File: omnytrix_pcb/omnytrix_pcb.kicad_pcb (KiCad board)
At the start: 2 copper layers, 38 x 45.5 mm, 37 parts, among them J1 Conn_01x07, J2 Micro_SD_Card_Det2, J3 Conn_01x02, J4 USB_C_Receptacle_PowerOnly_6P, SW1 SW_Push, U1 LD3985M33R_SOT23, U2 TP4056, U3 STM32F411RCTx, U4 FS8205A, U5 DW01

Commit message: add ground filled zone
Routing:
- net GND: vias 12 -> 32
- added copper zone on B.Cu, net GND
- added copper zone on F.Cu, net GND
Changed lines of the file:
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@@
   (segment (start 88.190736 105.434962) (end 85.731126 105.434962) (width 0.5) (layer "F.Cu") (net 2))
   (via (at 95.33886 94.532757) (size 0.8) (drill 0.4) (layers "F.Cu" "B.Cu") (net 2))
+  (via (at 83.455723 106.615239) (size 0.8) (drill 0.4) (layers "F.Cu" "B.Cu") (free) (net 2))
+  (via (at 85.177509 90.32317) (size 0.8) (drill 0.4) (layers "F.Cu" "B.Cu") (free) (net 2))
+  (via (at 112.594438 89.521213) (size 0.8) (drill 0.4) (layers "F.Cu" "B.Cu") (free) (net 2))
   (via (at 96.706297 116.206286) (size 0.8) (drill 0.4) (layers "F.Cu" "B.Cu") (net 2))
+  (via (at 98.209321 82.905062) (size 0.8) (drill 0.4) (layers "F.Cu" "B.Cu") (free) (net 2))
+  (via (at 104.166757 95.184021) (size 0.8) (drill 0.4) (layers "F.Cu" "B.Cu") (free) (net 2))
+  (via (at 89.939833 118.060929) (size 0.8) (drill 0.4) (layers "F.Cu" "B.Cu") (free) (net 2))
+  (via (at 109.855 118.745) (size 0.8) (drill 0.4) (layers "F.Cu" "B.Cu") (free) (net 2))
+  (via (at 110.890277 86.864728) (size 0.8) (drill 0.4) (layers "F.Cu" "B.Cu") (free) (net 2))
+  (via (at 102.01862 83.957631) (size 0.8) (drill 0.4) (layers "F.Cu" "B.Cu") (free) (net 2))
   (via (at 102.395827 116.206286) (size 0.8) (drill 0.4) (layers "F.Cu" "B.Cu") (net 2))
+  (via (at 107.95 85.725) (size 0.8) (drill 0.4) (layers "F.Cu" "B.Cu") (free) (net 2))
+  (via (at 108.654941 107.256118) (size 0.8) (drill 0.4) (layers "F.Cu" "B.Cu") (free) (net 2))
   (via (at 110.490014 92.074987) (size 0.8) (drill 0.4) (layers "F.Cu" "B.Cu") (free) (net 2))
+  (via (at 100.299291 96.078373) (size 0.8) (drill 0.4) (layers "F.Cu" "B.Cu") (free) (net 2))
   (via (at 103.698249 110.434498) (size 0.8) (drill 0.4) (layers "F.Cu" "B.Cu") (net 2))
+  (via (at 107.599133 88.101725) (size 0.8) (drill 0.4) (layers "F.Cu" "B.Cu") (free) (net 2))
+  (via (at 110.177288 121.594747) (size 0.8) (drill 0.4) (layers "F.Cu" "B.Cu") (free) (net 2))
   (via (at 93.499717 92.695613) (size 0.8) (drill 0.4) (layers "F.Cu" "B.Cu") (net 2))
+  (via (at 109.22 116.84) (size 0.8) (drill 0.4) (layers "F.Cu" "B.Cu") (free) (net 2))
+  (via (at 90.040078 123.023042) (size 0.8) (drill 0.4) (layers "F.Cu" "B.Cu") (free) (net 2))
   (via (at 94.317543 93.546819) (size 0.8) (drill 0.4) (layers "F.Cu" "B.Cu") (net 2))
+  (via (at 102.224128 85.712211) (size 0.8) (drill 0.4) (layers "F.Cu" "B.Cu") (free) (net 2))
   (via (at 116.840014 105.409987) (size 0.8) (drill 0.4) (layers "F.Cu" "B.Cu") (free) (net 2))
+  (via (at 105.95055 104.971373) (size 0.8) (drill 0.4) (layers "F.Cu" "B.Cu") (free) (net 2))
   (via (at 96.761135 112.874826) (size 0.8) (drill 0.4) (layers "F.Cu" "B.Cu") (net 2))
   (via (at 116.840014 95.249987) (size 0.8) (drill 0.4) (layers "F.Cu" "B.Cu") (free) (net 2))
+  (via (at 97.235271 98.171575) (size 0.8) (drill 0.4) (layers "F.Cu" "B.Cu") (free) (net 2))
   (via (at 99.869991 112.389477) (size 0.8) (drill 0.4) (layers "F.Cu" "B.Cu") (net 2))
+  (via (at 89.839589 120.416679) (size 0.8) (drill 0.4) (layers "F.Cu" "B.Cu") (free) (net 2))
   (via (at 98.296623 108.844171) (size 0.8) (drill 0.4) (layers "F.Cu" "B.Cu") (net 2))
   (segment (start 102.235014 116.204987) (end 102.415014 116.204987) (width 0.5) (layer "B.Cu") (net 2))
@@
   (segment (start 88.88548 96.046387) (end 88.874134 96.046387) (width 0.3) (layer "B.Cu") (net 69))
   (segment (start 90.544214 97.705121) (end 88.88548 96.046387) (width 0.3) (layer "B.Cu") (net 69))
+  (zone (net 2) (net_name "GND") (layers "F&B.Cu") (name "1") (hatch edge 0.5)
+    (connect_pads (clearance 0.5))
+    (min_thickness 0.25) (filled_areas_thickness no)
+    (fill yes (thermal_gap 0.5) (thermal_bridge_width 0.5))
+    (polygon
+      (pts
+        (xy 72.39 72.39)
+        (xy 128.27 71.12)
+        (xy 127.635 140.97)
+        (xy 71.755 135.255)
+      )
+    )
+  )
 )

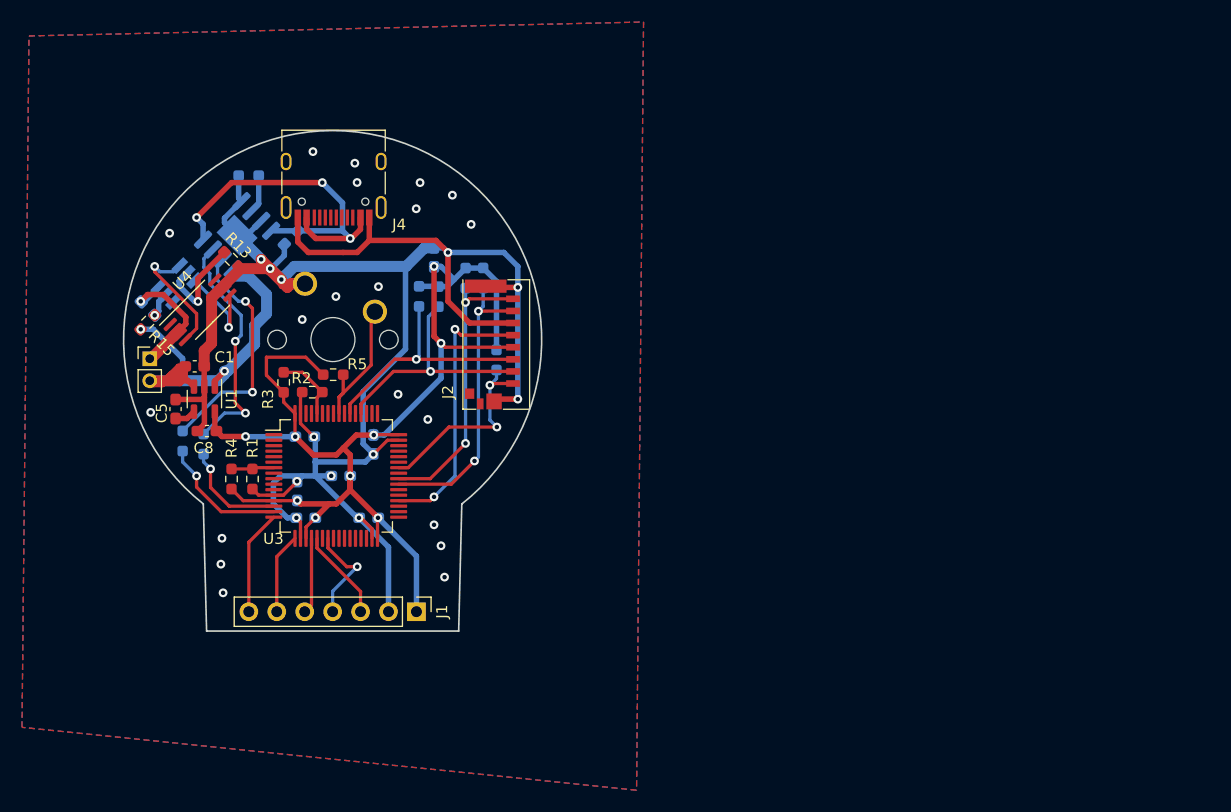
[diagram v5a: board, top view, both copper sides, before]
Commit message: add buzzer and encoder
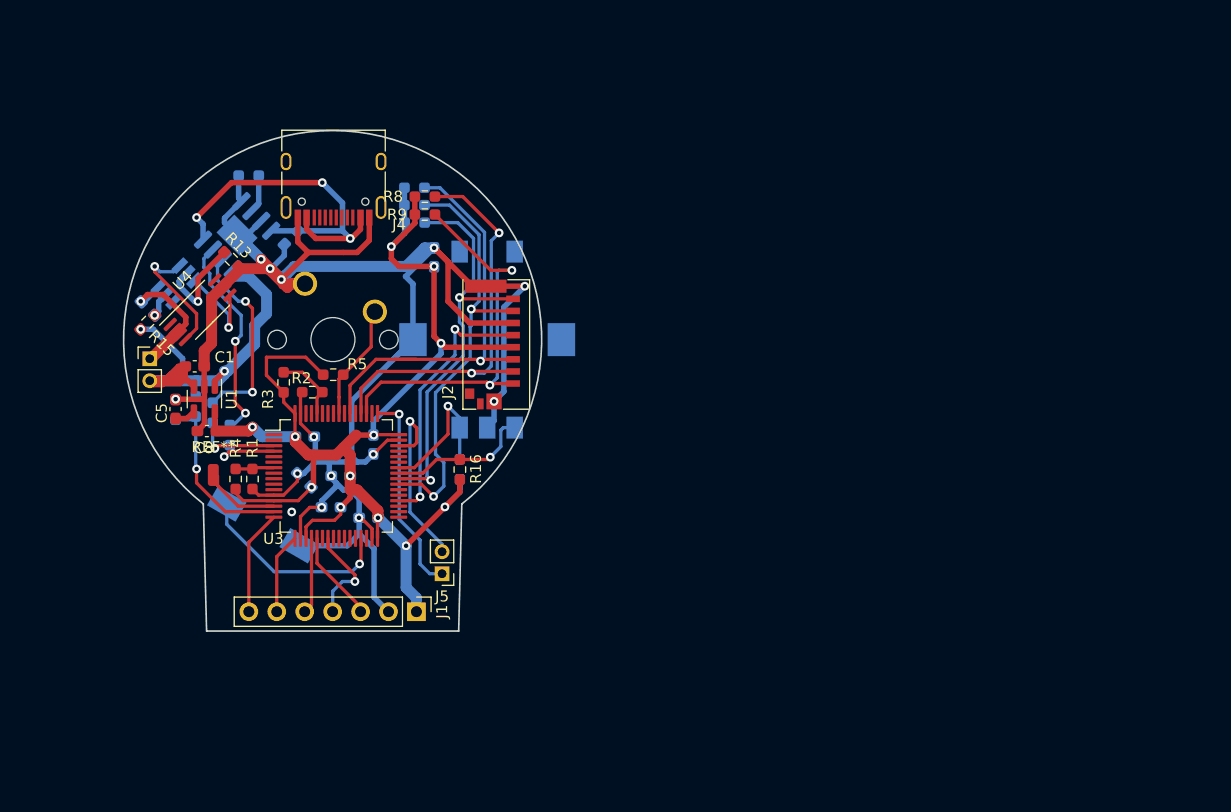
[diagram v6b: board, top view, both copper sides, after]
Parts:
- added J5: Conn_01x02, Connector_PinHeader_2.00mm:PinHeader_1x02_P2.00mm_Vertical, F.Cu at (110.0, 121.3)
- added LS1: Speaker, libs:smd_buzzer, B.Cu at (93.7, 116.8)
- added R16: 10k, Resistor_SMD:R_0603_1608Metric_Pad0.98x0.95mm_HandSolder, F.Cu at (111.6, 111.8)
- added R17: 10k, Resistor_SMD:R_0603_1608Metric_Pad0.98x0.95mm_HandSolder, B.Cu at (111.6, 111.8)
- added R18: 47k, Resistor_SMD:R_0603_1608Metric_Pad0.98x0.95mm_HandSolder, B.Cu at (87.6, 106.1)
- added R19: 47k, Resistor_SMD:R_0603_1608Metric_Pad0.98x0.95mm_HandSolder, B.Cu at (85.7, 106.4)
- added REF**: SolderWirePad_1x01_SMD_1x2mm, Connector_Wire:SolderWirePad_1x01_SMD_1x2mm, F.Cu at (89.2, 112.3)
- added SW2: RotaryEncoder_Switch, libs:EC11_encoder, B.Cu at (114.1, 100.0)
- R8, R9: moved to F.Cu
- moved R9 14.7 mm to (108.4, 88.6), turned to 0 degrees
- moved R10 9.89 mm to (107.4, 86.2), turned to 0 degrees
- moved R8 9.18 mm to (108.4, 87.0), turned to 0 degrees
- moved R7 9.11 mm to (107.4, 87.8), turned to 0 degrees
- moved R6 6.85 mm to (107.5, 89.4), turned to 0 degrees
- moved R11 3.74 mm to (89.1, 106.7)
- moved R12 2.52 mm to (90.6, 108.7)
- moved C9 2.49 mm to (99.9, 115.2)
- moved C7 1.17 mm to (97.4, 112.8), turned to 135 degrees
- moved R4 0.38 mm to (91.2, 112.7)
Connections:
- U3 pad 14: /CHRG -> unconnected-(U3-PA0-Pad14)
- U3 pad 15: /STDBY -> Net-(U3-PA1)
- U3 pad 29: unconnected-(U3-PB10-Pad29) -> /BUZZER
- U3 pad 3: unconnected-(U3-PC14-Pad3) -> /STDBY
- U3 pad 4: unconnected-(U3-PC15-Pad4) -> /CHRG
- U3 pad 41: unconnected-(U3-PA8-Pad41) -> /encoder_a
- U3 pad 42: /SD_D2 -> /encoder_b
- U3 pad 46: unconnected-(U3-PA13-Pad46) -> /SWDIO
- U3 pad 49: unconnected-(U3-PA14-Pad49) -> /SWCL
- U3 pad 51: unconnected-(U3-PC10-Pad51) -> /SD_D2
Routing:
- net /SWCL: track 0.00 -> 18.8 mm, vias 0 -> 1
- net /BUZZER: track 0.00 -> 18.4 mm, vias 0 -> 1
- net /SD_D2: track 18.3 -> 36.6 mm
- net /SWDIO: track 0.00 -> 17.0 mm, vias 0 -> 1
- net /SD_D3: track 22.3 -> 38.5 mm, vias 1 -> 2
- net Net-(U3-PA1): track 0.00 -> 16.1 mm, vias 0 -> 1
- net /SD_CMD: track 24.3 -> 39.5 mm
- net /encoder_b: track 0.00 -> 13.6 mm, vias 0 -> 1
- net +3.3V: track 113.6 -> 126.9 mm, vias 9 -> 12
- net /encoder_a: track 0.00 -> 13.1 mm, vias 0 -> 1
- net /SD_D0: track 27.0 -> 39.7 mm
- net /SD_D1: track 26.0 -> 37.2 mm
- net unconnected-(U3-PA0-Pad14): track 0.00 -> 6.76 mm
- net /CHRG: track 10.2 -> 5.98 mm
- net /STDBY: track 11.8 -> 7.88 mm
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- removed copper zone on B.Cu, net GND
- removed copper zone on F.Cu, net GND

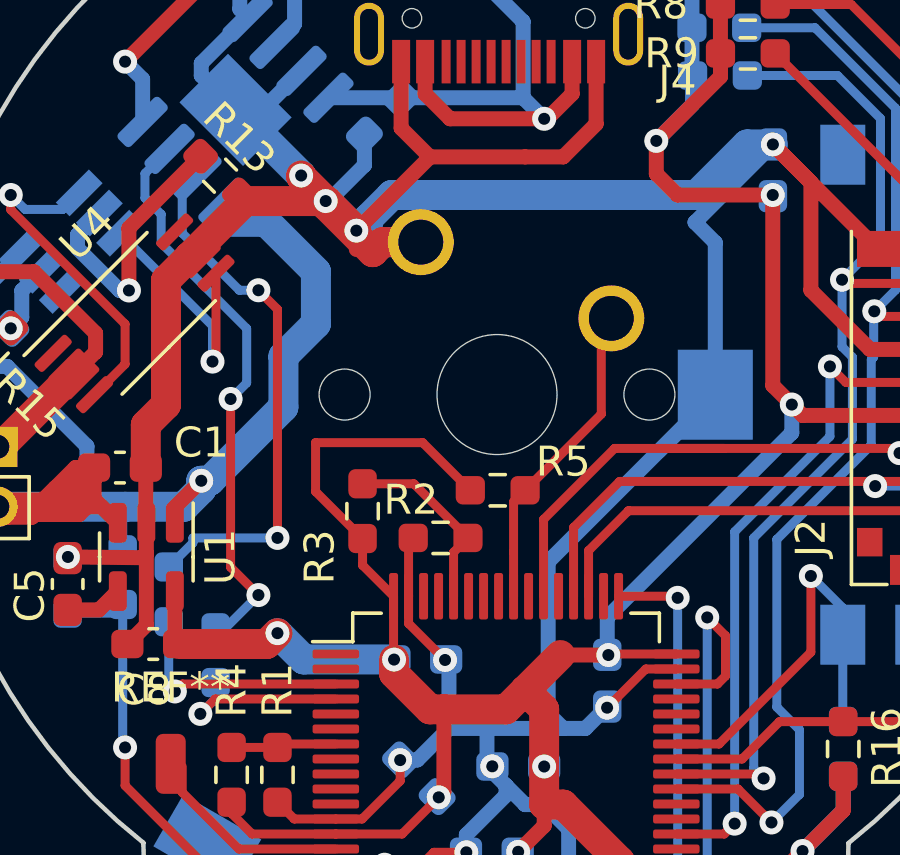
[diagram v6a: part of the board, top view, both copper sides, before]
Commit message: add vbat for rtc
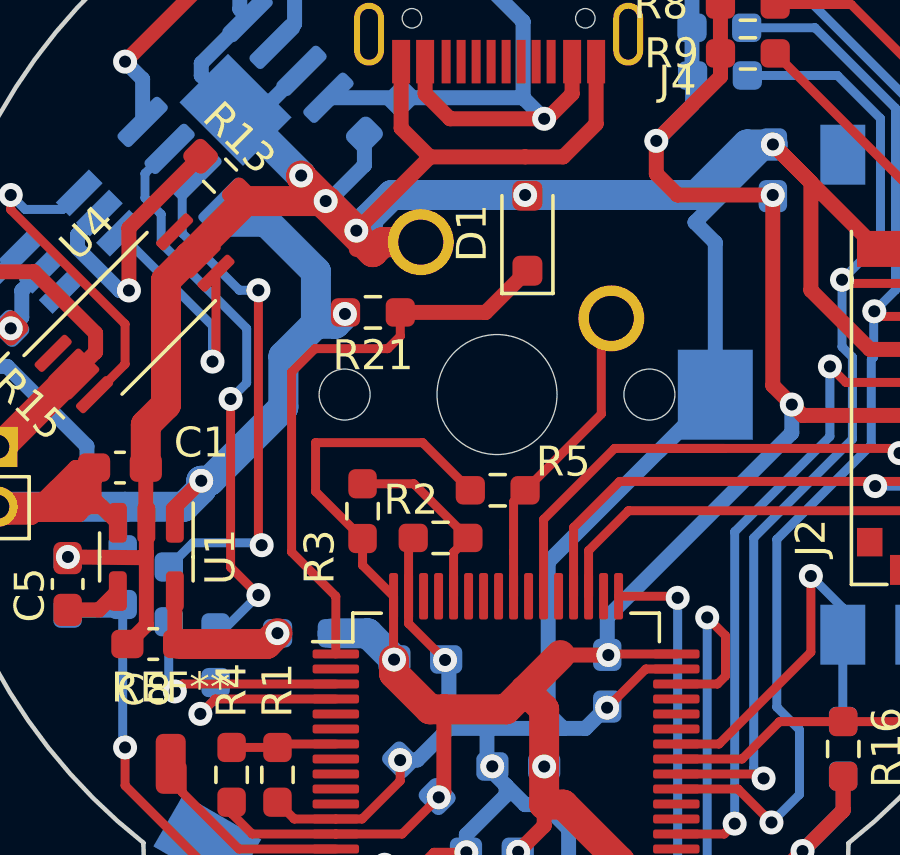
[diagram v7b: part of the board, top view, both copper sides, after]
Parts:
- added D1: D_Zener, Diode_SMD:D_SOD-323_HandSoldering, F.Cu at (101.0, 94.6)
- added R20: 0, Resistor_SMD:R_0603_1608Metric_Pad0.98x0.95mm_HandSolder, B.Cu at (93.6, 108.0)
- added R21: 10k, Resistor_SMD:R_0603_1608Metric_Pad0.98x0.95mm_HandSolder, F.Cu at (95.9, 97.3)
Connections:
- C8 pad 1: +3.3V -> Net-(U1-VOUT)
- U1 pad 5: +3.3V -> Net-(U1-VOUT)
- U3 pad 1: unconnected-(U3-VBAT-Pad1) -> Net-(D1-K)
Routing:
- net Net-(D1-K): track 0.00 -> 19.7 mm
- net +3.3V: track 126.9 -> 119.7 mm, vias 12 -> 11
- net Net-(U1-VOUT): track 0.00 -> 5.41 mm, vias 0 -> 1
- net +BATT: track 49.9 -> 51.0 mm, vias 2 -> 3
- net Net-(U2-~{STDBY}): track 18.1 -> 17.4 mm
- net GND: vias 13 -> 14
